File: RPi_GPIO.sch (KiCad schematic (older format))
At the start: 1 part, among them J2 RPi_GPIO

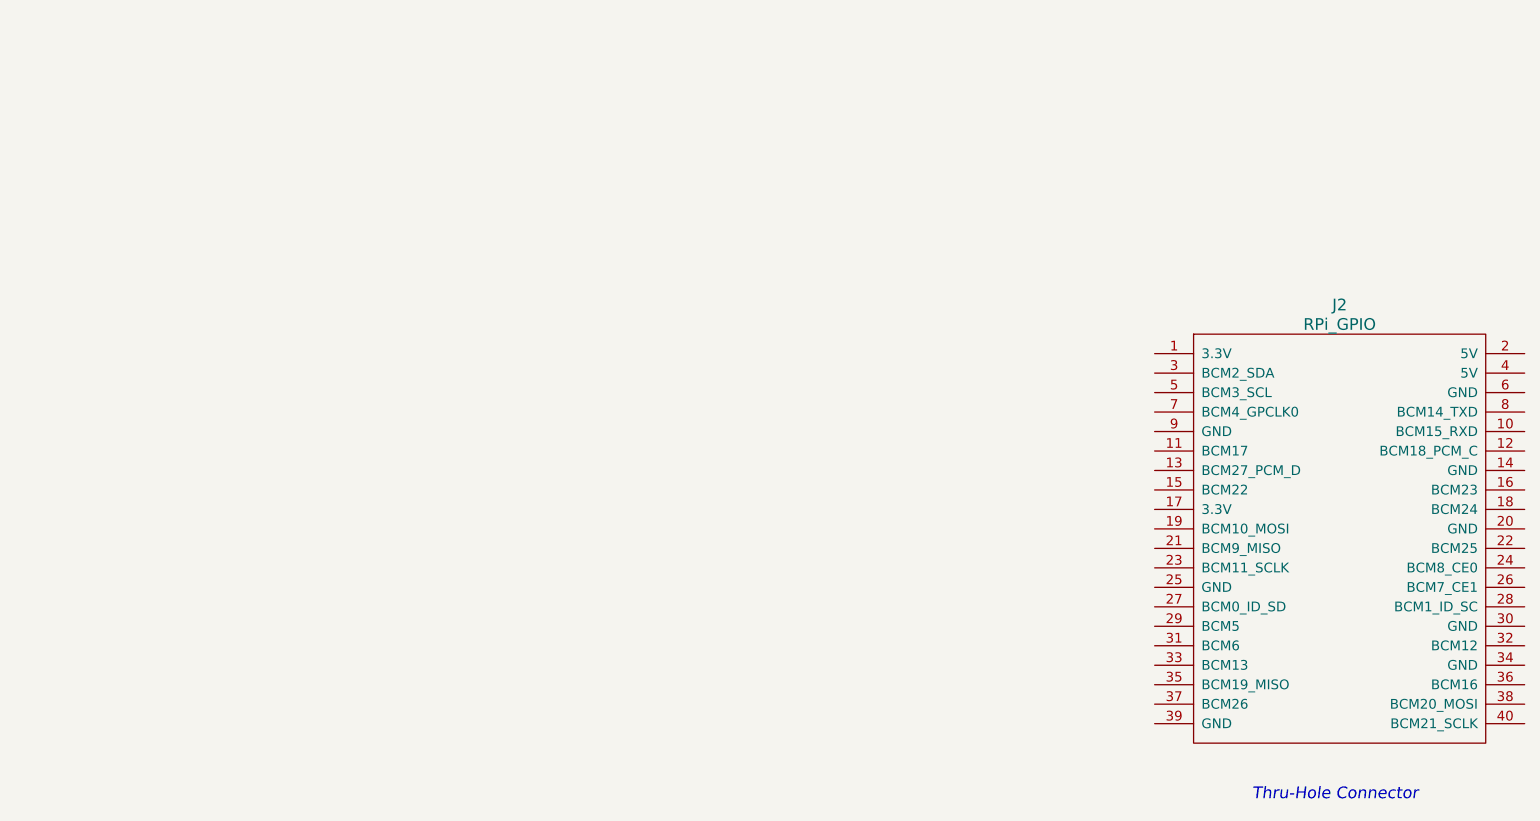
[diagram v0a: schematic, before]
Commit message: Added components to schematic
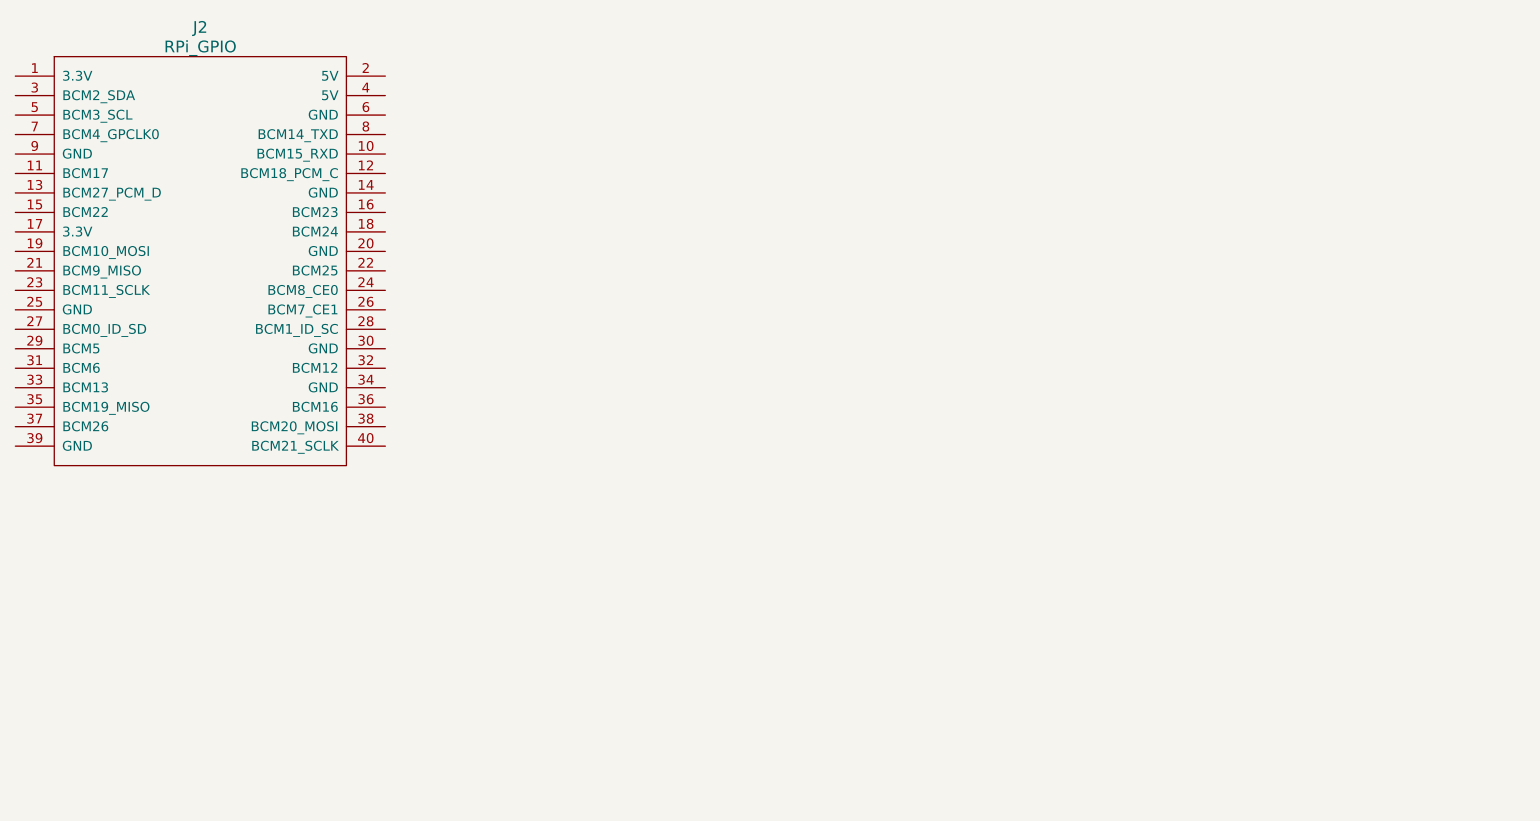
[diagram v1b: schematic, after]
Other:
- note removed: "Thru-Hole Connector"
- moved on the sheet: J2
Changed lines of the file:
@@
 L RPi_GPIO J2
 U 1 1 5516AE26
-P 7500 2700
+P 1650 1275
 AR Path="/5516AE26" Ref="J2"  Part="1"
 AR Path="/5515D395/5516AE26" Ref="J2"  Part="1"
-F 0 "J2" H 8250 2950 60  0000 C CNN
-F 1 "RPi_GPIO" H 8250 2850 60  0000 C CNN
-F 2 "RPi_Hat:Pin_Header_Straight_2x20" H 7500 2700 60  0001 C CNN
-F 3 "" H 7500 2700 60  0000 C CNN
-	1    7500 2700
+F 0 "J2" H 2400 1525 60  0000 C CNN
+F 1 "RPi_GPIO" H 2400 1425 60  0000 C CNN
+F 2 "RPi_Hat:Pin_Header_Straight_2x20" H 1650 1275 60  0001 C CNN
+F 3 "" H 1650 1275 60  0000 C CNN
+	1    1650 1275
 	1    0    0    -1
 $EndComp
-Text Notes 7800 5000 0    60   Italic 0
-Thru-Hole Connector
 $EndSCHEMATC
